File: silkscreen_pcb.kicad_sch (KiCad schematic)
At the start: 184 parts, among them J1 USB_C_Receptacle, J2 FH34SRJ-24S-0.5SH_50_, J3 FH34SRJ-6S-0.5SH_50_, J4 FH34SRJ-6S-0.5SH_50_, J5 Conn_01x02, J6 PPPC062LJBN-RC, J7 Micro_SD_Card, Q1 FS8205A, Q2 AO3401A, Q3 AO3401A, Q4 IRLML6346TRPBF, Q5 BSS138, Q6 BSS138, Q7 AO3401A, Q8 AO3401A, Q9 BSS138, SW1 SW_Push, SW10 SW_Push, SW11 SW_Push, SW2 SW_Push, SW3 SW_Push, SW4 SW_Push, SW5 SW_Push, SW6 SW_Push, SW7 SW_Push, SW8 SW_Push, SW9 SW_Push, U1 TPD4E1U06DBVR, U10 TPS923610DRLR, U11 TP4056-42-ESOP8, U12 74LVC1G04, U13 DS3231MZ, U14 RV-8263-C7, U2 TPS2116DRL, U3 TLV75533PDBV, U4 ESP32-S3-WROOM-1, U5 DW01A, U6 TPD4E1U06DBVR, U7 TPD4E1U06DBVR, U8 TPD4E1U06DBVR, U9 TPD4E1U06DBVR

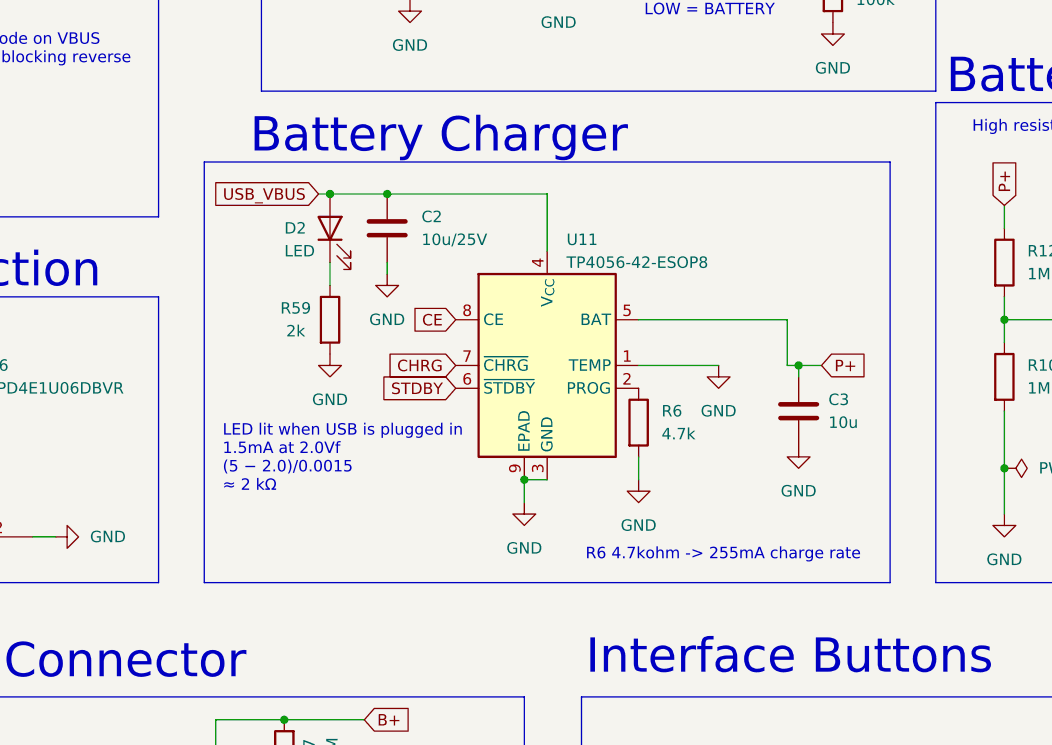
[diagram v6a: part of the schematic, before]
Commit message: Rev 1.01: R84 USB hot-plug damper, JLC placement corrections, docs
- R84, 1 ohm 0603 (Yageo RC0603FR-071RL; JLC C22936, Basic) in series with
  C2's ground leg. It damps the ringing an already-live USB-A source causes
  at plug-in: the modelled worst case on U2 VIN1 falls from 7.95 V to 5.60 V.
  No DC current flows in it. One GND stitching via below the cut line moved
  to make room (a board trimmed at y 62 still shows 0 unconnected); the CHRG
  track is nudged 0.2 mm.
- FT Rotation Offset (U2, U5, D2, D8) and FT Position Offset (J7, J4, U4)
  fields on the symbols and footprints, so every Toolkit run writes
  positions.csv rows that match JLC's library footprints.
- Bottom silkscreen notes enlarged; R83, R67 and C3 reference texts moved;
  D3's description reads 26.0 Vr.
- production/ regenerated (zip SHA-256 5b819f11..., 166 placed parts, 67
  LCSC codes) and checked: DRC 0 unconnected / 0 parity, Gerbers and drills
  match a fresh kicad-cli export as shape sets, netlist.ipc matches a fresh
  IPC-D-356. jlc_bom.csv, part_fields.csv and other_fabs updated; schematic
  and layout PDFs re-plotted.
- Docs: README, HARDWARE.md (hot-plug in section 3.1), DESIGN_REVIEW.md,
  fabrication README/BOM/NextPCB notes, the 2026-09-30 audit banner and
  BRING_UP section 3.2. New docs/LED_ALT.md: the TPS923610 alternate-driver
  study.
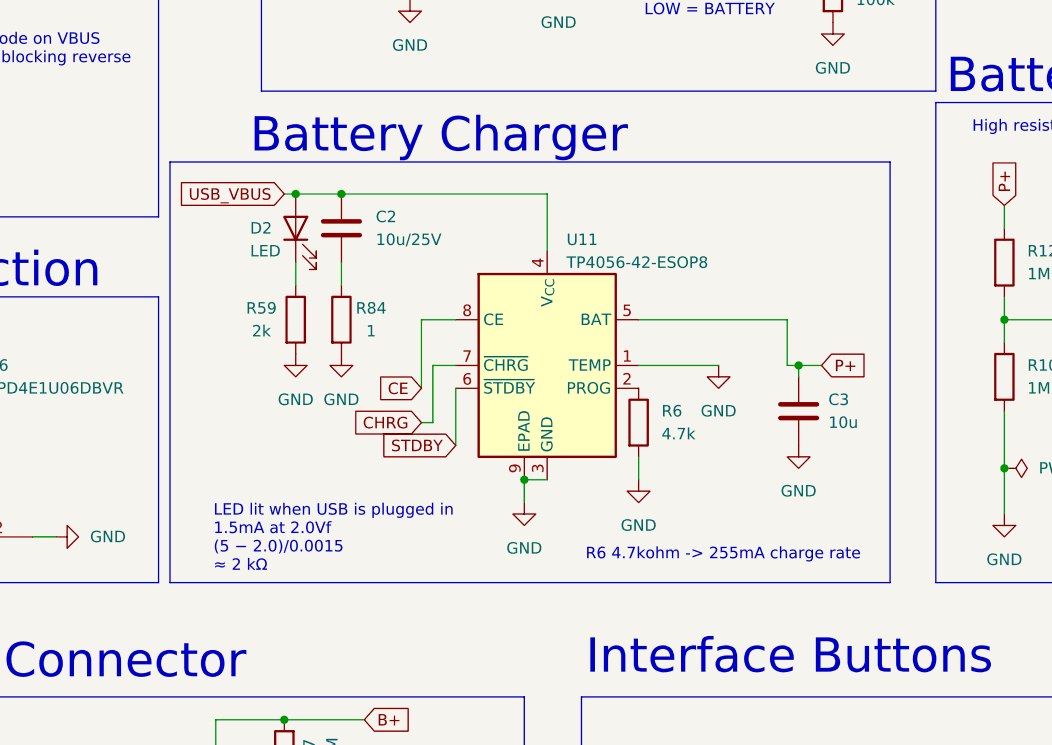
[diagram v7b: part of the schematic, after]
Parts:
- added R84: 1, Resistor_SMD:R_0603_1608Metric_Pad0.98x0.95mm_HandSolder, symbol Device:R
- D2, D8: FT Rotation Offset (none) -> 180
- J4: FT Position Offset (none) -> -0.73,0.218
- J7: FT Position Offset (none) -> 1.6,-5.3
- U2: FT Rotation Offset (none) -> -90
- U4: FT Position Offset (none) -> 0,-3.664
- U5: FT Rotation Offset (none) -> 90
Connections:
- net GND: now also R84.2; no longer C2.2
- new net: C2.2, R84.1
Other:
- moved on the sheet: C2, D2, R59

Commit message: Rev 1.02: SMD USB-C socket with hand-solder pads, charge-enable gate from USB_VBUS, docs and cost data
Rev 1.01 was never built, so these changes are labelled 1.02 and replace it.

Board and fabrication files
- J1 is now the 12-pad SMD GCT USB4105 land (JLC C2765186, Shou Han; prime part
  USB4105-GF-A) instead of the through-hole USB4085. Its nets, the shield ring and the four
  long edge traces are re-routed. The four J1 hole-clearance DRC findings (pegs against the
  stacked GND pads) are excluded in the project file.
- J1's CPL row carries FT Position Offset 0,1.305, because JLC's footprint origin sits 1.305 mm
  from KiCad's (read from JLC's own footprint); no rotation offset.
- Each J1 pad has a 0.3 mm copper-and-mask extension behind it (0.2 mm at A8), with no paste,
  so the socket can be hand-soldered. The original pads, paste apertures and 0.2 mm mask dams
  are unchanged.
- Charge-enable gate (Q2, R81) is fed from USB_VBUS instead of 3V3; R79/R80/R81/R82 are now
  1M/10M/100k/10k (about 10 uA less sleep current by calculation). The 3V3 copper that fed
  the gate is removed. The 1 um 3V3 stub is gone.
- Top VBUS run straightened and a ground via added next to J1.
- Title blocks are Rev 1.02 (2026-10-22).
- production/ regenerated: Silkscreen_Reader_PCB_1.02.zip (the 1.01 zip is removed), BOM,
  CPL, IPC netlist, NextPCB and PCBWay files, assembly drawing. Both PDFs re-plotted.

BOMs and cost data
- part_fields.csv, jlc_bom.csv, bom.csv, the hand-build DigiKey BOM (J1 USB4105-GF-A $0.80)
  and the other-fab BOMs carry the new J1 and R79-R82 values.
- fabrication/BOM.md: the cost table is re-run on the current jlc_bom.csv with JLC library
  prices of 2026-10-23 (per board at 5/10/30/100 boards: $32.48 / $23.03 / $15.58 / $11.94,
  25 Extended types), with the figures that depend on it.

Docs
- README, HARDWARE, DESIGN_REVIEW, fabrication README and BOM, BRING_UP and the audit notes
  describe Rev 1.02 and keep Rev 1.0 / 1.01 as history.
- New: docs/audit-202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
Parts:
- J1: footprint Connector_USB:USB_C_Receptacle_GCT_USB4085 -> Connector_USB:USB_C_Receptacle_GCT_USB4105-xx-A_16P_TopMnt_Horizontal; FT Position Offset (none) -> 0,1.305; LCSC C7095263 -> C2765186; MPN USB4085-GF-A -> USB4105-GF-A
- R79: value 100k -> 1M; LCSC C25803 -> C22935; MPN RC0603FR-07100KL -> RC0603FR-071ML
- R80: value 1M -> 10M; LCSC C22935 -> C7250; MPN RC0603FR-071ML -> RC0603FR-0710ML
- R81: value 1M -> 100k; LCSC C22935 -> C25803; MPN RC0603FR-071ML -> RC0603FR-07100KL
- R82: value 1M -> 10k; LCSC C22935 -> C25804; MPN RC0603FR-071ML -> RC0603FR-0710KL
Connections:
- net 3V3: no longer Q2.2 (S), R81.2
- net USB_VBUS: now also Q2.2 (S), R81.2
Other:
- note added: "R6 4.7kohm -> ~234mA charge rate"
- note removed: "R6 4.7kohm -> 255mA charge rate"
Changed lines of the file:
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@@
 	(title_block
 		(title "Silkscreen Reader PCB")
-		(date "2026-09-30")
-		(rev "1.01")
+		(date "2026-10-22")
+		(rev "1.02")
 		(company "idc LLC")
 		(comment 1 "Open-hardware e-reader base board")
@@
 		)
 	)
-	(text "R6 4.7kohm -> 255mA charge rate"
+	(text "R6 4.7kohm -> ~234mA charge rate"
 		(exclude_from_sim no)
 		(at 149.098 123.952 0)
@@
 		)
 	)
-	(text_box "TPS923 chip is a series LED boost converter. \nRecommended to run between 10kHz-25kHz via PWM_LED for brightness control.\nPWM_LED (ADIM) is also the ENABLE: first HIGH pulse must be >= 40 us (tADIM_EN), so hold HIGH >= 100 us\nbefore starting the PWM carrier; LOW for > 2.5 ms (tADIM_SD) shuts the driver down.\nReturn path for LEDs is toggled via COLOR_SEL for warm/cool selection.\nFeedback current is ~13.3mA tuned via R37. Reference datasheet to change as needed.\nLED_MONIT is analog signal that references 0-24.5V output on LED voltage. (ADC range from 0 to ~30V)\nInternal OVP should cut out at ~24V, but software protection should kick in and disable LED_ACTIVATE at safe voltage above known forward voltage (15V)\nAfter 3 OVP trips the driver LATCHES off: re-applying PWM will not restart it - hold PWM_LED LOW > 2.5 ms (or power-cycle).\nChange COLOR_SEL only with PWM duty at 0. Never enable with J3 unplugged."
+	(text_box "TPS923 chip is a series LED boost converter. \nRecommended to run between 10kHz-25kHz via PWM_LED for brightness control.\nPWM_LED (ADIM) is also the ENABLE: first HIGH pulse must be >= 40 us (tADIM_EN), so hold HIGH >= 100 us\nbefore starting the PWM carrier; LOW for > 2.5 ms (tADIM_SD) shuts the driver down.\nReturn path for LEDs is toggled via COLOR_SEL for warm/cool selection.\nFeedback current is ~13.3mA tuned via R37. Reference datasheet to change as needed.\nLED_MONIT is analog signal that references 0-24.5V output on LED voltage. (ADC range from 0 to ~30V)\nInternal OVP should cut out at ~24V, but software protection should kick in and disable PWM_LED at safe voltage above known forward voltage (15V)\nAfter 3 OVP trips the driver LATCHES off: re-applying PWM will not restart it - hold PWM_LED LOW > 2.5 ms (or power-cycle).\nChange COLOR_SEL only with PWM duty at 0. With no light connected, LED_MONIT (software trip ~23V) and the U10 OVP latch protect the driver; avoid enabling it with J3 and J6 empty."
 		(exclude_from_sim no)
 		(at 233.68 308.61 0)
@@
 		)
 	)
-	(global_label "3V3"
+	(global_label "USB_VBUS"
 		(shape input)
 		(at 114.3 190.5 0)
@@
 			)
 		)
-		(property "Footprint" "Connector_USB:USB_C_Receptacle_GCT_USB4085"
+		(property "Footprint" "Connector_USB:USB_C_Receptacle_GCT_USB4105-xx-A_16P_TopMnt_Horizontal"
 			(at 36.83 45.72 0)
 			(effects
@@
 			)
 		)
-		(property "MPN" "USB4085-GF-A"
+		(property "MPN" "USB4105-GF-A"
 			(at 33.02 45.72 0)
 			(effects
@@
 			)
 		)
-		(property "LCSC" "C7095263"
+		(property "LCSC" "C2765186"
+			(at 33.02 45.72 0)
+			(effects
+				(font
+					(size 1.27 1.27)
+				)
+				(hide yes)
+			)
+		)
+		(property "FT Position Offset" "0,1.305"
 			(at 33.02 45.72 0)
 			(effects
@@
 			)
 		)
-		(property "Value" "100k"
+		(property "Value" "1M"
 			(at 92.71 201.93 90)
 			(effects
@@
 			)
 		)
-		(property "MPN" "RC0603FR-07100KL"
+		(property "MPN" "RC0603FR-071ML"
 			(at 92.71 204.47 0)
 			(effects
@@
 			)
 		)
-		(property "LCSC" "C25803"
+		(property "LCSC" "C22935"
 			(at 92.71 204.47 0)
 			(effects
@@
 			)
 		)
-		(property "Value" "1M"
+		(property "Value" "100k"
 			(at 104.648 196.85 0)
 			(effects
@@
 			)
 		)
-		(property "MPN" "RC0603FR-071ML"
+		(property "MPN" "RC0603FR-07100KL"
 			(at 107.95 195.58 0)
 			(effects
@@
 			)
 		)
-		(property "LCSC" "C22935"
+		(property "LCSC" "C25803"
 			(at 107.95 195.58 0)
 			(effects
@@
 			)
 		)
-		(property "Value" "1M"
+		(property "Value" "10k"
 			(at 114.808 180.34 0)
 			(effects
@@
 			)
 		)
-		(property "MPN" "RC0603FR-071ML"
+		(property "MPN" "RC0603FR-0710KL"
 			(at 118.11 179.07 0)
 			(effects
@@
 			)
 		)
-		(property "LCSC" "C22935"
+		(property "LCSC" "C25804"
 			(at 118.11 179.07 0)
 			(effects
@@
 			)
 		)
-		(property "Value" "1M"
+		(property "Value" "10M"
 			(at 97.028 209.55 0)
 			(effects
@@
 			)
 		)
-		(property "MPN" "RC0603FR-071ML"
+		(property "MPN" "RC0603FR-0710ML"
 			(at 100.33 208.28 0)
 			(effects
@@
 			)
 		)
-		(property "LCSC" "C22935"
+		(property "LCSC" "C7250"
 			(at 100.33 208.28 0)
 			(effects
